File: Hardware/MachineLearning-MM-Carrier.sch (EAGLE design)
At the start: 47 parts, among them J11 microSD, J2 JTAG, J3 QWIIC_RIGHT_ANGLE, J9 MICROMOD-2222-C, U5 AP7361C-33FGE

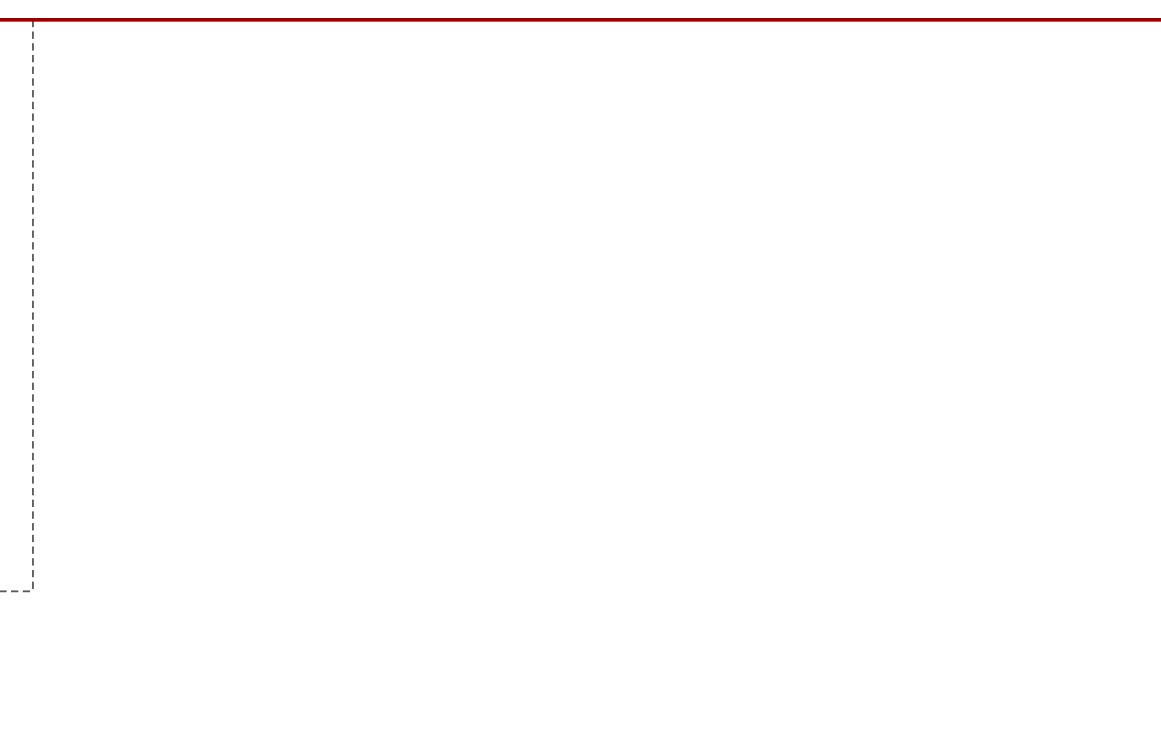
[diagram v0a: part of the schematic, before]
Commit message: Added BME280 block
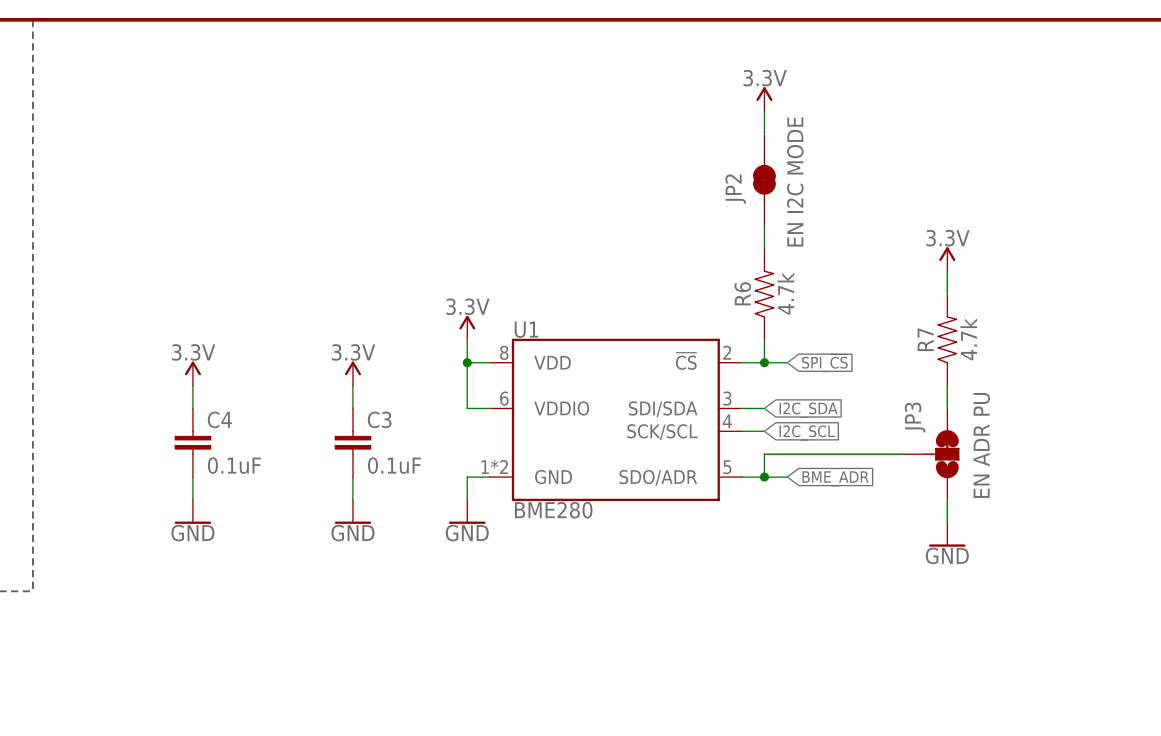
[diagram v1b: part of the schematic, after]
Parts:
- added C3, C4: 0.1uF, SparkFun-Capacitors:0.1UF-0603-100V-10%
- added JP2: EN I2C MODE, SparkFun-Jumpers:JUMPER-SMT_2_NC_TRACE_SILK
- added JP3: EN ADR PU, SparkFun-Jumpers:JUMPER-SMT_3_1-NC_TRACE_SILK
- added R6, R7: 4.7k, SparkFun-Resistors:4.7KOHM-0603-1/10W-1%
- added U1: BME280, SparkFun-Sensors:BME280
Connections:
- new net BME_ADR: JP3.2, U1.SDO/ADR
- new net N$5: JP2.1, R6.2
- new net N$8: JP3.3, R7.1
- net 3.3V: now also C3.1, C4.1, JP2.2, R7.2, U1.VDD, U1.VDDIO
- net GND: now also C3.2, C4.2, JP3.1, U1.GND
- net I2C_SCL: now also U1.SCK/SCL
- net I2C_SDA: now also U1.SDI/SDA
- net SPI_!CS!: now also R6.1, U1.!CS
